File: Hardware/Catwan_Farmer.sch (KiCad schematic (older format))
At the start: 49 parts, among them J1 SENSOR 1, J10 VSP, J2 SENSOR 2, J3 SENSOR 3, J4 BATT, J5 USB_B, J6 SWD, J7 DHT22, J9 SENSOR 4, SW1 RST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

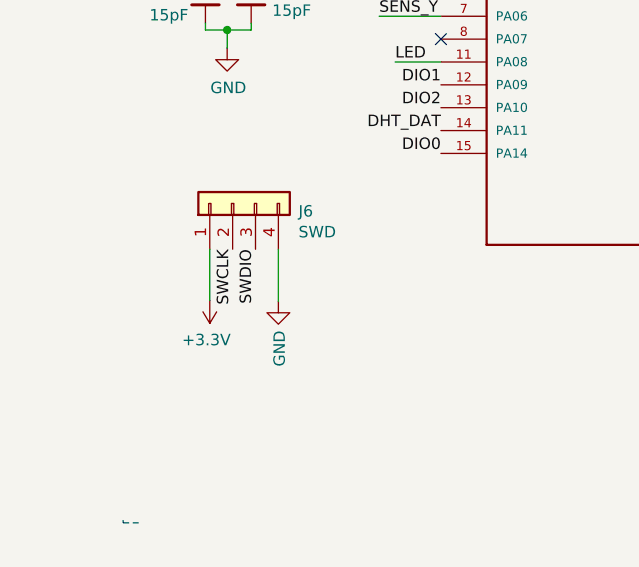
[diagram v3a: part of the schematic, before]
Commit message: Change DI0 and CLK
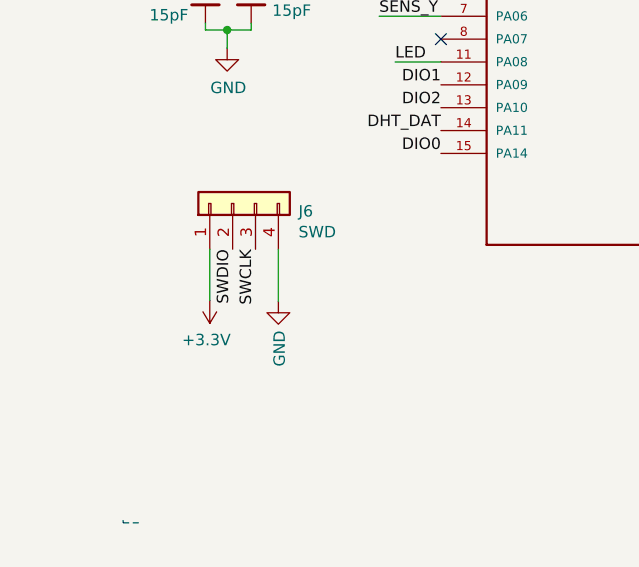
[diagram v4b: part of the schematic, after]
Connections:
- net SWCLK: now also J6.3 (Pin_3); no longer J6.2 (Pin_2)
- net SWDIO: now also J6.2 (Pin_2); no longer J6.3 (Pin_3)
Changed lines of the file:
@@
 EESchema Schematic File Version 4
+LIBS:Catwan_Farmer-cache
 EELAYER 30 0
 EELAYER END
@@
 Text Label 3200 1960 0    50   ~ 0
 S0
-Text Label 889  3279 3    50   ~ 0
+Text Label 989  3279 3    50   ~ 0
 SWCLK
 Text Label 1296 6057 2    50   ~ 0
@@
 	0    -1   -1   0
 $EndComp
-Text Label 989  3279 3    50   ~ 0
+Text Label 889  3279 3    50   ~ 0
 SWDIO
 Wire Wire Line
